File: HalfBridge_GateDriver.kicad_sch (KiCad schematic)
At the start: 8 parts, among them U1 UCC21520ADW, U2 TBA2-0522, U3 TBA2-0522

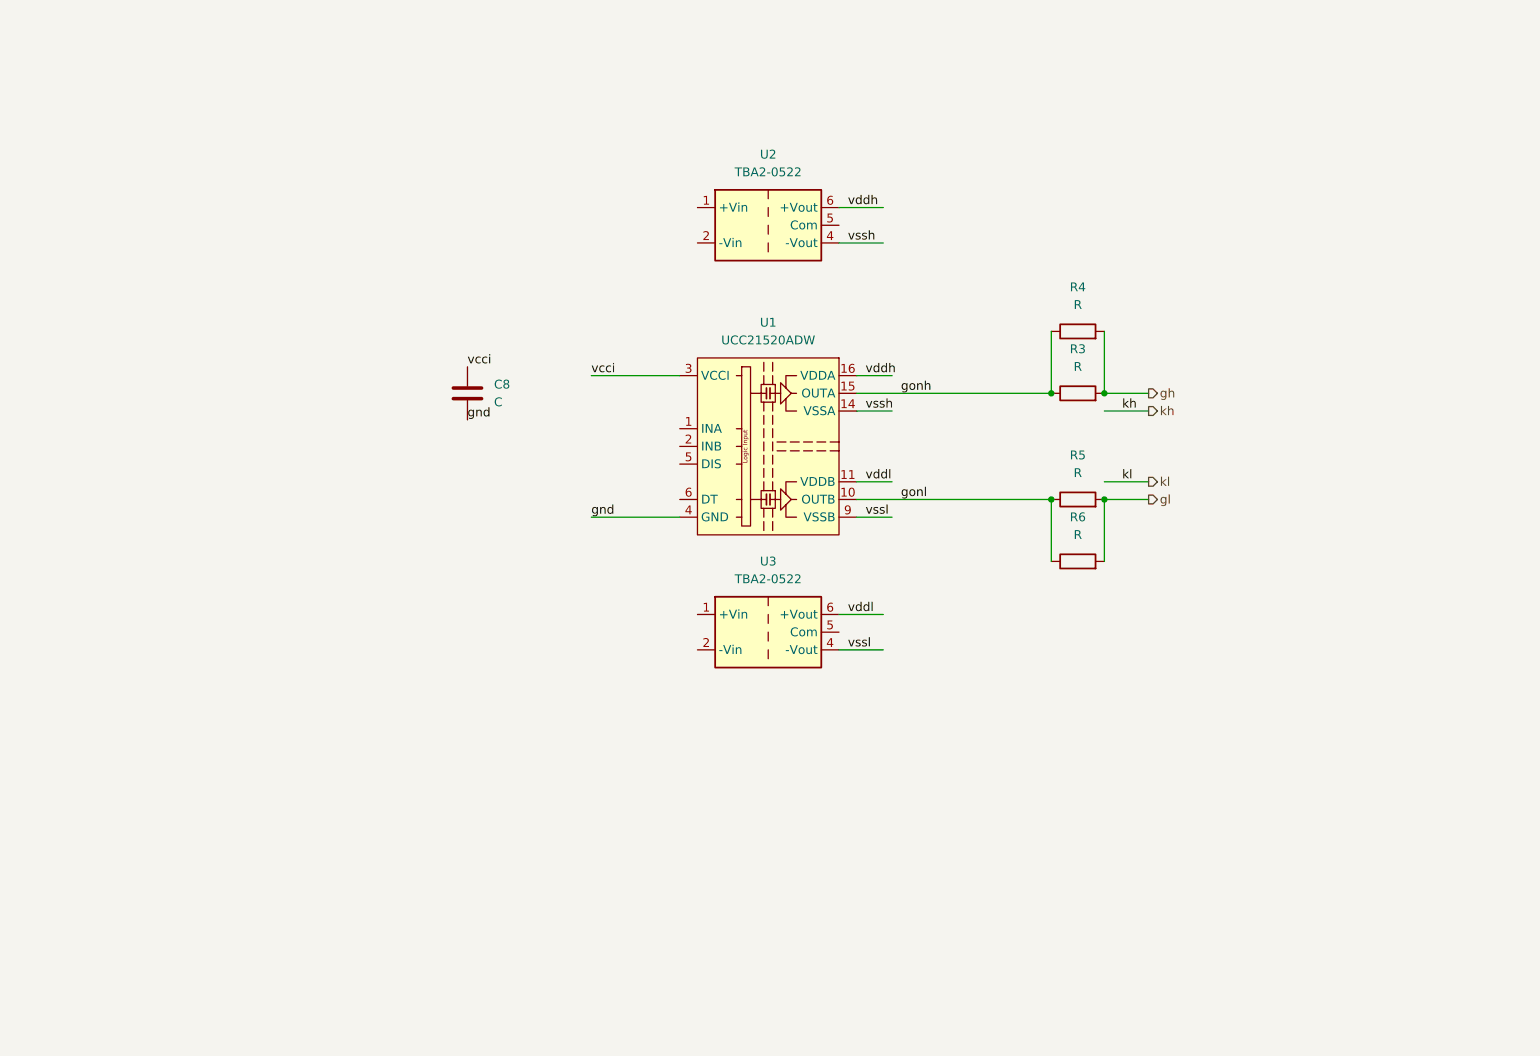
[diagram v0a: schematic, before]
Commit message: gate driver
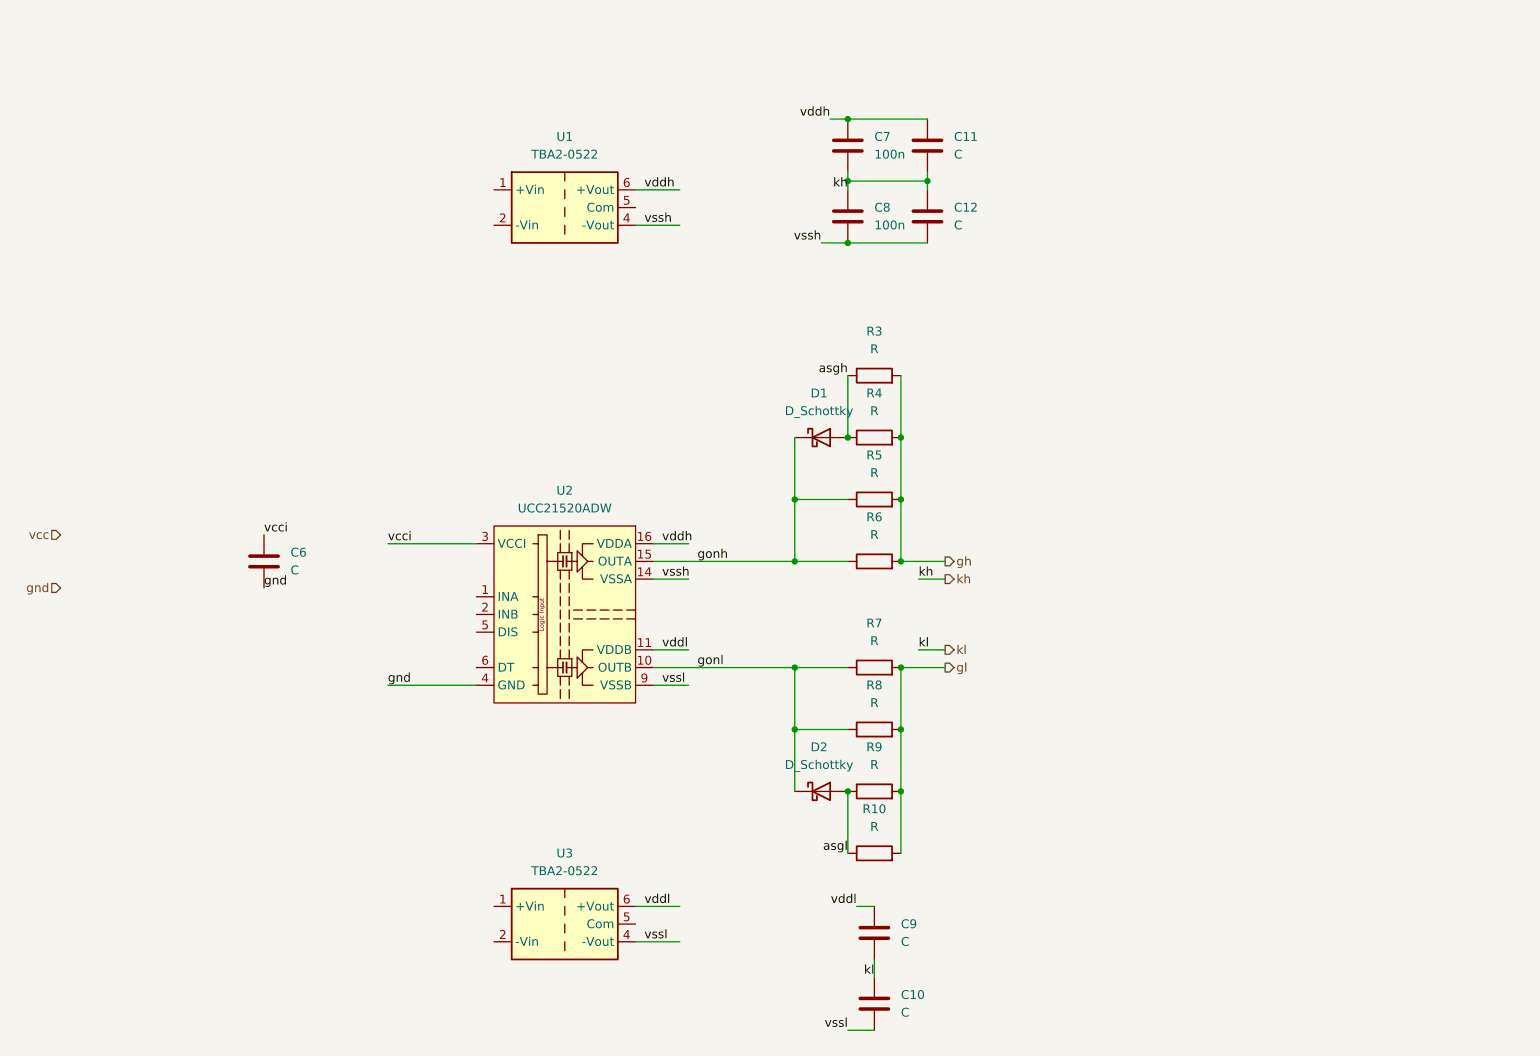
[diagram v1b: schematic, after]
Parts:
- added C10, C9: C, Capacitor_SMD:C_0603_1608Metric_Pad1.08x0.95mm_HandSolder, symbol Device:C
- added C11, C12: C, Capacitor_SMD:C_0805_2012Metric_Pad1.18x1.45mm_HandSolder, symbol Device:C
- added C7, C8: 100n, Capacitor_SMD:C_0603_1608Metric_Pad1.08x0.95mm_HandSolder, symbol Device:C
- added D1, D2: D_Schottky, Diode_SMD:D_SOD-123, symbol Device:D_Schottky
- added R10, R3, R5, R9: R, Resistor_SMD:R_0805_2012Metric_Pad1.20x1.40mm_HandSolder, symbol Device:R
- renumbered C8 to C6, R3 to R6, R5 to R7, R6 to R8, U2 to U1, U1 to U2
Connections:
- net gh: now also R3.2, R5.2
- net gl: now also R10.2, R9.2
- net gonh: now also D1.1 (K), R5.1; no longer R4.1
- net gonl: now also D2.1 (K)
- net kh: now also C11.2, C12.1, C7.2, C8.1
- net kl: now also C10.1, C9.2
- net vddh: now also C11.1, C7.1
- net vddl: now also C9.1
- net vssh: now also C12.2, C8.2
- net vssl: now also C10.2
- new net asgh: D1.2 (A), R3.1, R4.1
- new net asgl: D2.2 (A), R10.1, R9.1
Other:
- moved on the sheet: C6, R4, R6, R7, R8, U1, U2, U3

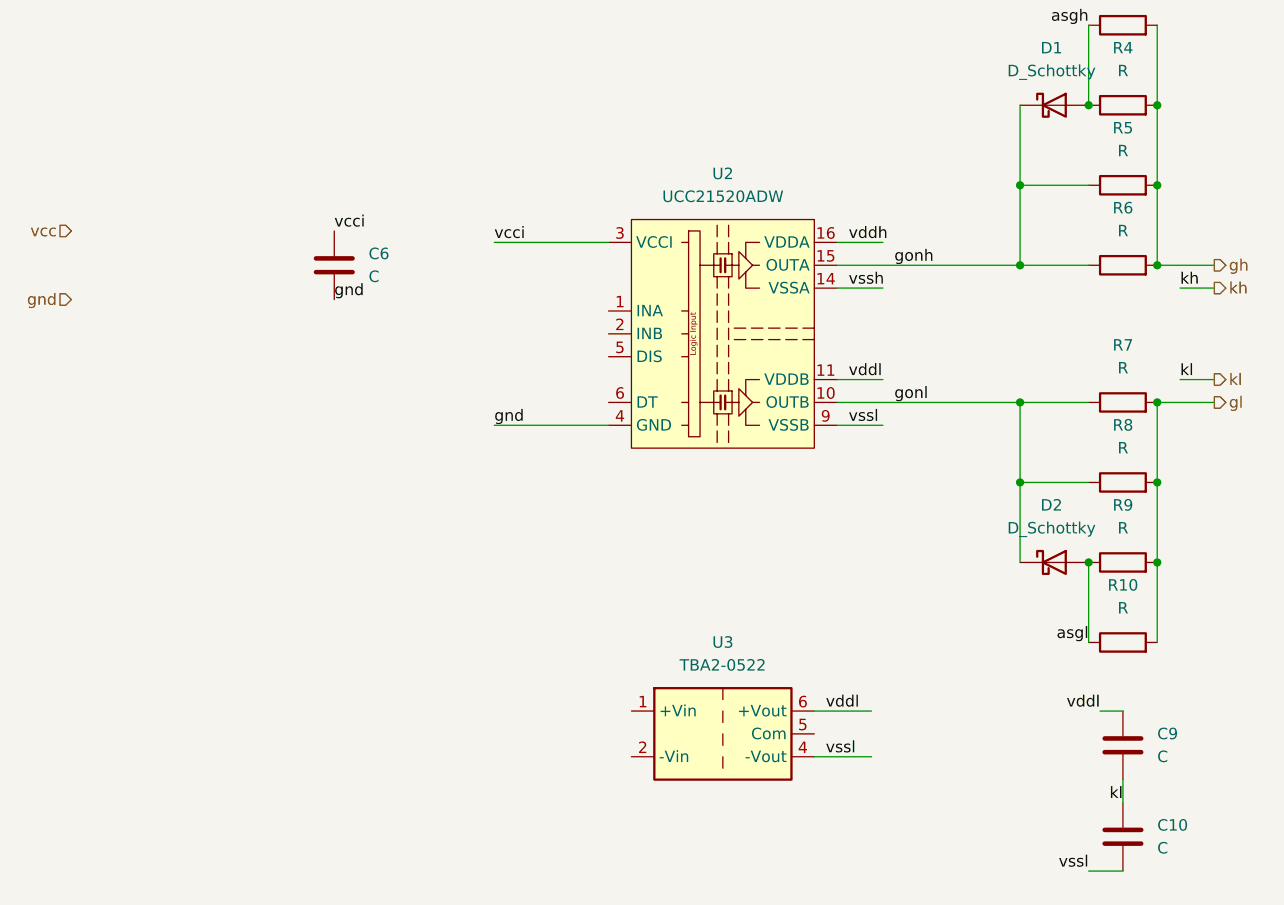
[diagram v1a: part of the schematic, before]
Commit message: symbol library gatedriver
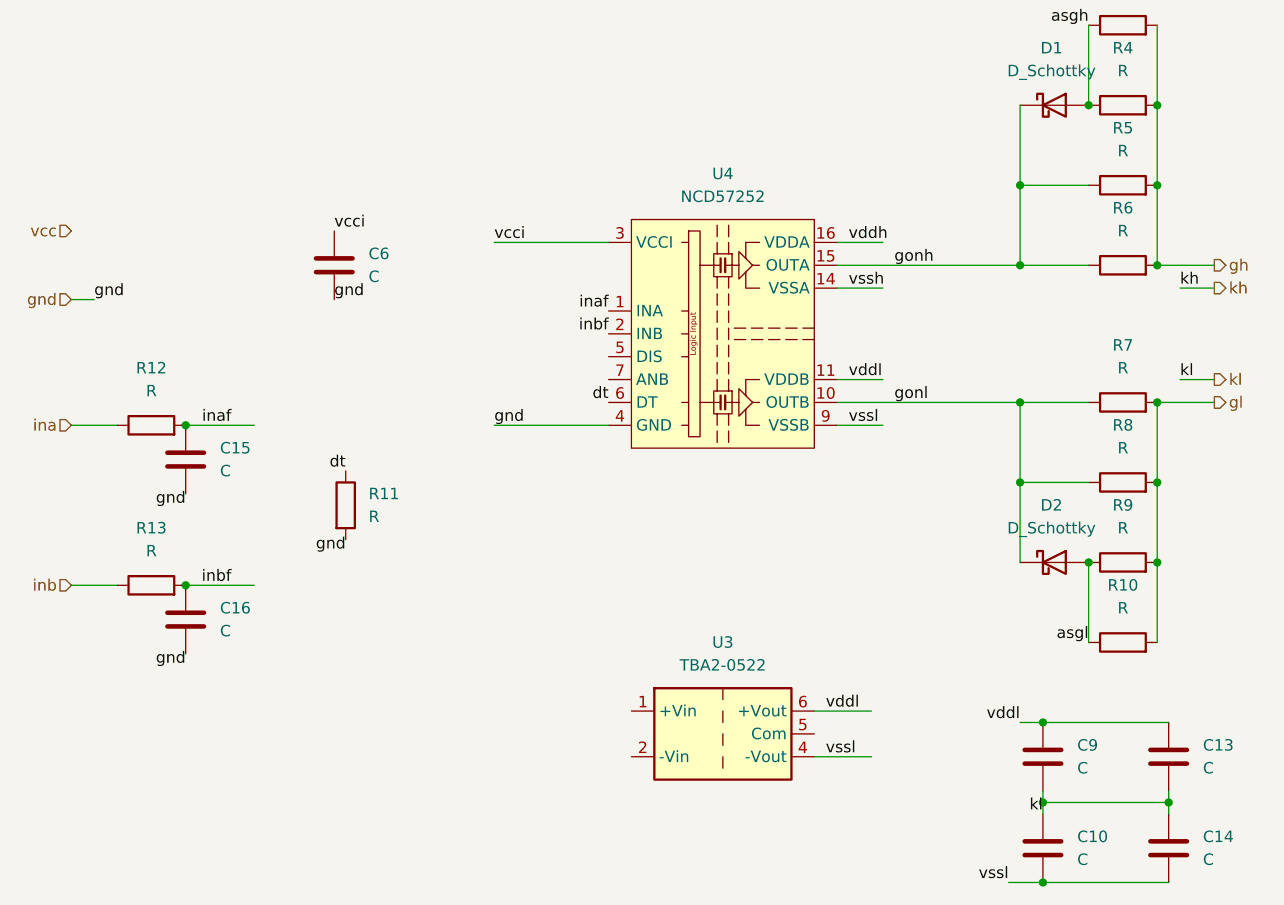
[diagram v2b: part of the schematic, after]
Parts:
- removed U2: UCC21520ADW, Package_SO:SOIC-16W_7.5x10.3mm_P1.27mm, symbol Driver_FET:UCC21520ADW
- added C13, C14: C, Capacitor_SMD:C_0805_2012Metric_Pad1.18x1.45mm_HandSolder, symbol Device:C
- added C15, C16: C, Capacitor_SMD:C_0603_1608Metric_Pad1.08x0.95mm_HandSolder, symbol Device:C
- added R11, R12, R13: R, Resistor_SMD:R_0603_1608Metric_Pad0.98x0.95mm_HandSolder, symbol Device:R
- added U4: NCD57252, Package_SO:SOIC-16W_7.5x10.3mm_P1.27mm, symbol My_Driver_FET:NCD57252
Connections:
- net gnd: now also C15.2, C16.2, R11.2, U4.4 (GND)
- net gonh: now also U4.15 (OUTA)
- net gonl: now also U4.10 (OUTB)
- net kl: now also C13.2, C14.1
- net vcci: now also U4.3 (VCCI), U4.8 (VCCI)
- net vddh: now also U4.16 (VDDA)
- net vddl: now also C13.1, U4.11 (VDDB)
- net vssh: now also U4.14 (VSSA)
- net vssl: now also C14.2, U4.9 (VSSB)
- new net dt: R11.1, U4.6 (DT)
- new net ina: R12.1
- new net inaf: C15.1, R12.2, U4.1 (INA)
- new net inb: R13.1
- new net inbf: C16.1, R13.2, U4.2 (INB)
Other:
- moved on the sheet: C10, C9

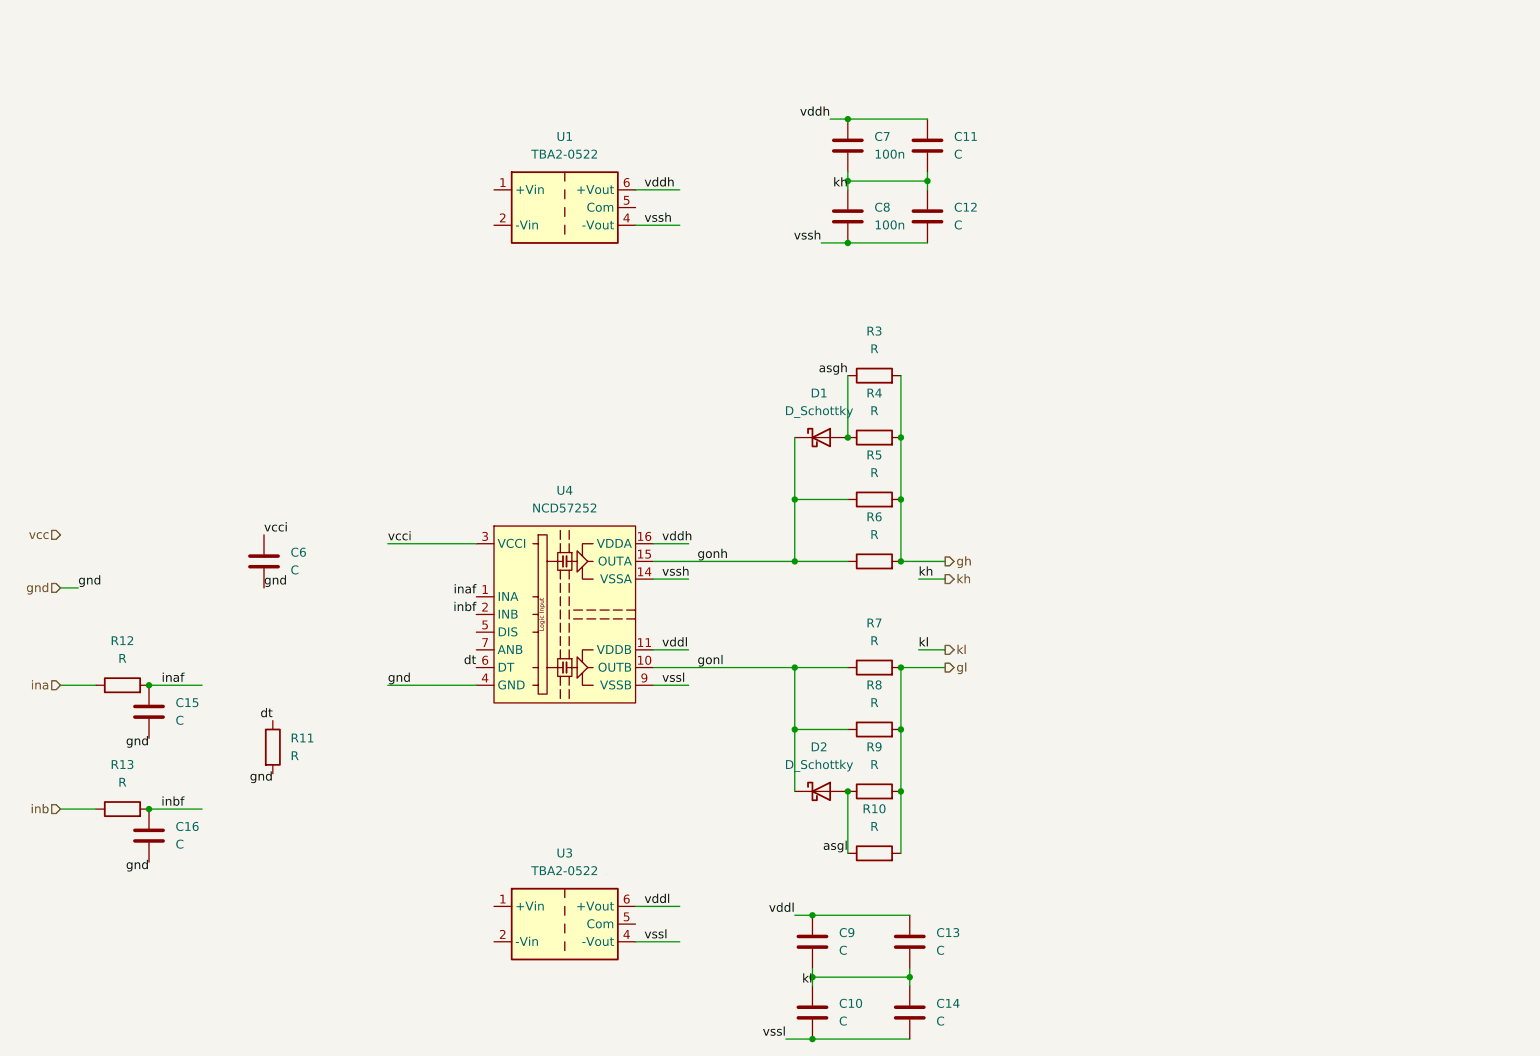
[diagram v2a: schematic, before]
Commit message: switch dpdt 3d model
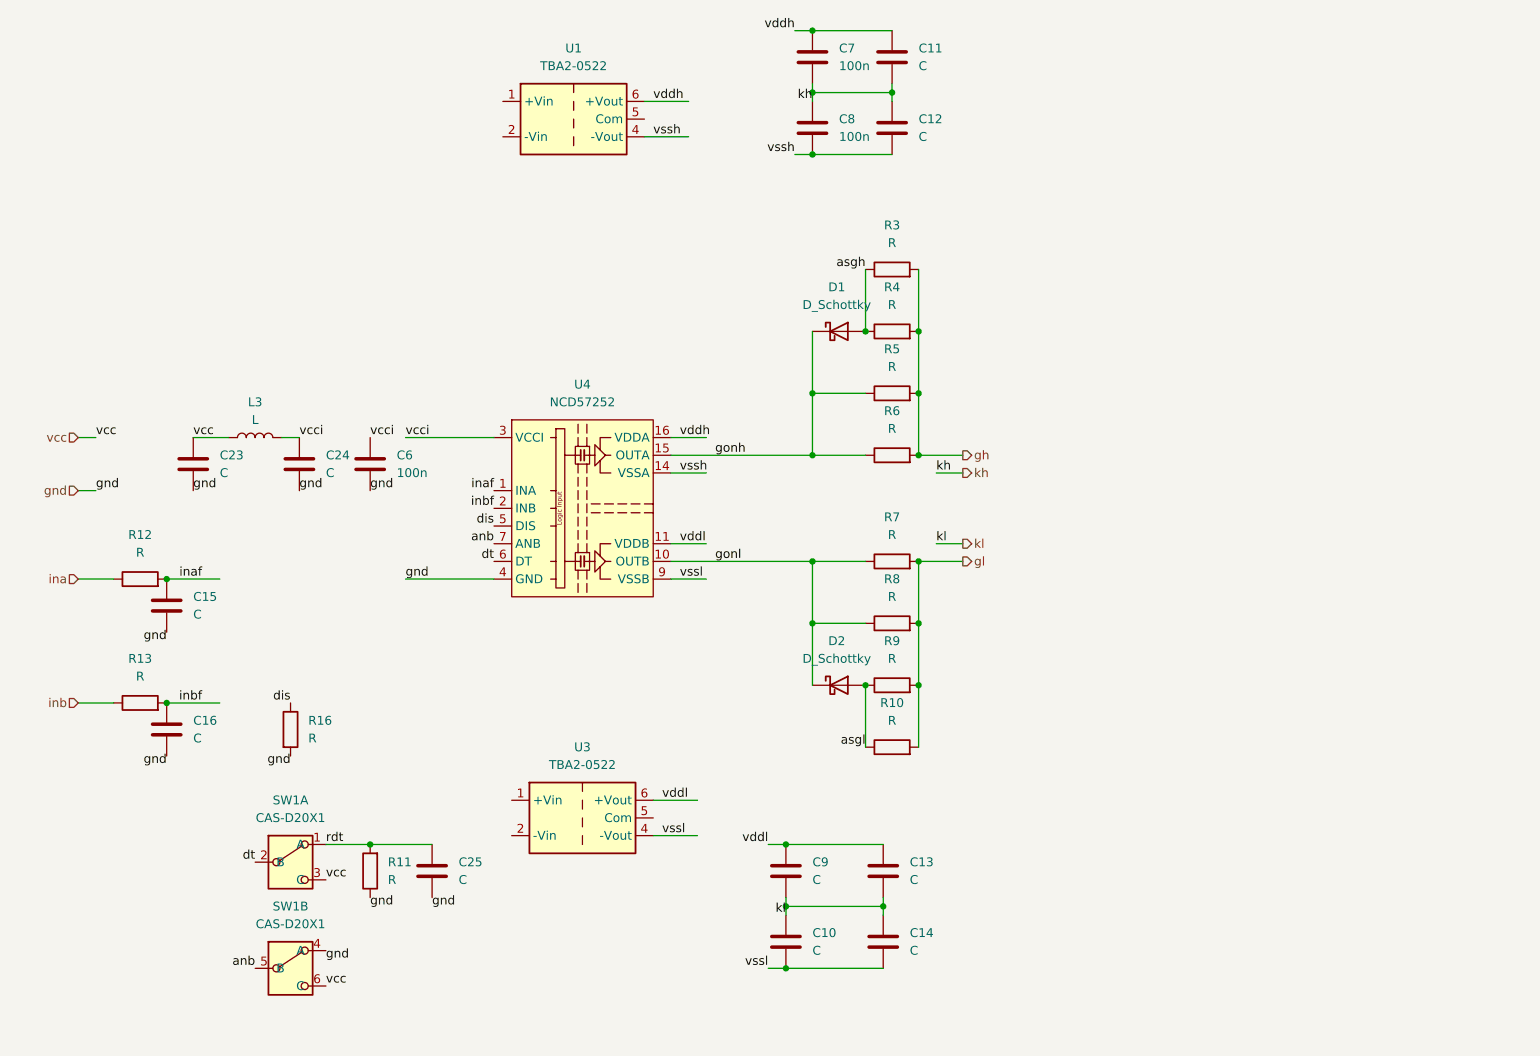
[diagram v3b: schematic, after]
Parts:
- added C23, C24: C, Capacitor_SMD:C_0805_2012Metric_Pad1.18x1.45mm_HandSolder, symbol Device:C
- added C25: C, Capacitor_SMD:C_0603_1608Metric_Pad1.08x0.95mm_HandSolder, symbol Device:C
- added L3: L, Inductor_SMD:L_0603_1608Metric_Pad1.05x0.95mm_HandSolder, symbol Device:L
- added R16: R, Resistor_SMD:R_0603_1608Metric_Pad0.98x0.95mm_HandSolder, symbol Device:R
- added SW1: CAS-D20X1, My_Button_Switch_SMD:Nidec_Copal_CAS-D20A1, symbol My_Switch:CAS-D20X1
- C6: value C -> 100n
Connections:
- net dt: now also SW1.2 (B); no longer R11.1
- net gnd: now also R11.1, C23.2, C24.2, C25.2, R16.2, SW1.4 (A); no longer R11.2
- net vcc: now also C23.1, L3.1, SW1.3 (C), SW1.6 (C)
- net vcci: now also C24.1, L3.2
- net dis: now reaches U4.5 (DIS)
- net dis: now also R16.1
- net anb: now reaches U4.7 (ANB)
- net anb: now also SW1.5 (B)
- new net rdt: C25.1, R11.2, SW1.1 (A)
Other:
- moved on the sheet: C10, C11, C12, C13, C14, C15, C16, C6, C7, C8, C9, D1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
